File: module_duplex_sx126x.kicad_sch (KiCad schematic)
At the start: 34 parts, among them J1 USB_B_Mini, J2 Conn_01x08_Pin, J3 Conn_01x05, J4 Conn_01x04, J6 Conn_01x02, SW1 SW_Push, U1 STM32F103C8Tx, U2 AMS1117-3.3, U3 SN65HVD230, U4 Ai-Thinker-Ra-02, U5 Ai-Thinker-Ra-02, Y1 16M, Y2 32.768k

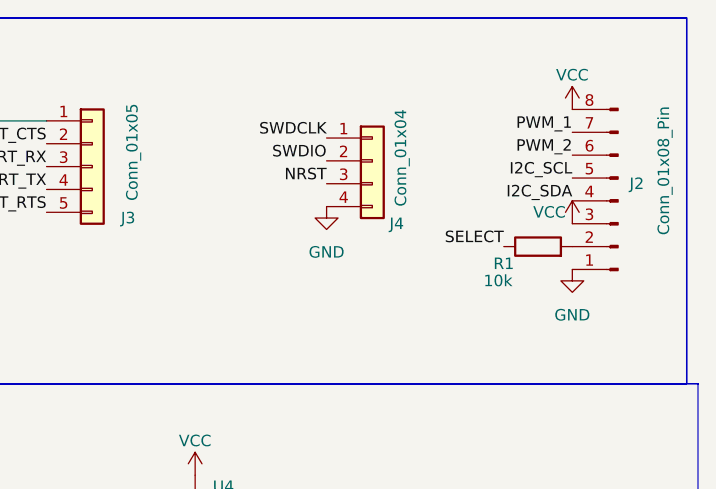
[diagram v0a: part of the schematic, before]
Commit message: Reduced expansion pins by simplifying select function with pull up/down
Signed-off-by: Leonardo Celente <leocelente@gmail.com>
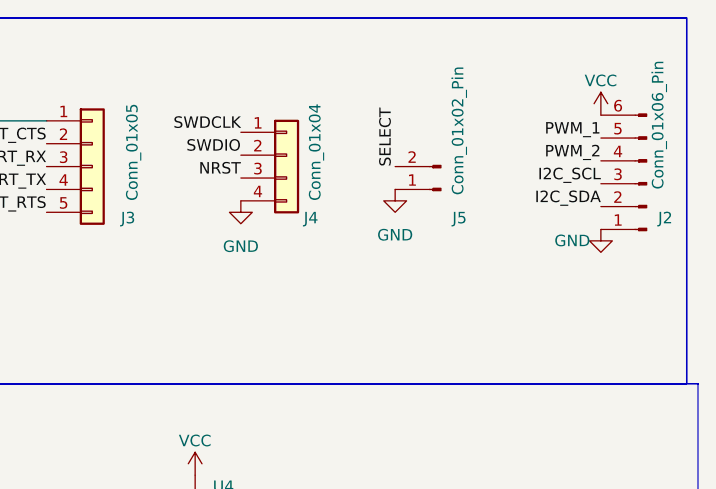
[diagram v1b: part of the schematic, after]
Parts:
- removed J2: Conn_01x08_Pin, Connector_PinHeader_2.54mm:PinHeader_1x08_P2.54mm_Vertical, symbol Connector:Conn_01x08_Pin
- removed R1: 10k, Resistor_SMD:R_0603_1608Metric, symbol Device:R
- added J2: Conn_01x06_Pin, Connector_PinHeader_2.54mm:PinHeader_1x06_P2.54mm_Vertical, symbol Connector:Conn_01x06_Pin
- added J5: Conn_01x02_Pin, Connector_PinHeader_2.54mm:PinHeader_1x02_P2.54mm_Vertical, symbol Connector:Conn_01x02_Pin
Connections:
- net GND: now also J2.1 (Pin_1), J5.1 (Pin_1)
- net I2C_SCL: now also J2.3 (Pin_3)
- net I2C_SDA: now also J2.2 (Pin_2)
- net PWM_1: now also J2.5 (Pin_5)
- net PWM_2: now also J2.4 (Pin_4)
- net SELECT: now also J5.2 (Pin_2)
- net VCC: now also J2.6 (Pin_6)
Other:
- moved on the sheet: J4

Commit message: Added USB resistors
Signed-off-by: Leonardo Celente <leocelente@gmail.com>
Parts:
- added R1, R4: 22, Resistor_SMD:R_0603_1608Metric, symbol Device:R
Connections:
- net USB_DM: now also R4.2; no longer J1.2 (D-)
- net USB_DP: now also R1.2; no longer J1.3 (D+)
- new net: J1.3 (D+), R1.1
- new net: J1.2 (D-), R4.1
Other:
- moved on the sheet: J1
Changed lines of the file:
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@@
   (no_connect (at 240.03 138.43))
   (no_connect (at 240.03 146.05))
-  (no_connect (at 119.38 43.18))
-  (no_connect (at 129.54 38.1))
+  (no_connect (at 111.125 43.18))
+  (no_connect (at 121.285 38.1))
   (no_connect (at 240.03 140.97))
   (no_connect (at 154.94 29.21))
@@
     (effects (font (size 1.27 1.27)) (justify right bottom))
   )
-  (label "USB_DM" (at 129.54 35.56 0) (fields_autoplaced)
+  (label "USB_DM" (at 128.905 35.56 0) (fields_autoplaced)
     (effects (font (size 1.27 1.27)) (justify left bottom))
   )
@@
     (effects (font (size 1.27 1.27)) (justify left bottom))
   )
-  (label "USB_DP" (at 129.54 33.02 0) (fields_autoplaced)
+  (label "USB_DP" (at 128.905 33.02 0) (fields_autoplaced)
     (effects (font (size 1.27 1.27)) (justify left bottom))
   )
@@
     )
   )
-  (symbol (lib_id "Connector:USB_B_Mini") (at 121.92 33.02 0) (unit 1)
+  (symbol (lib_id "Device:R") (at 125.095 33.02 90) (unit 1)
     (in_bom yes) (on_board yes) (dnp no) (fields_autoplaced)
-    (property "Reference" "J1" (at 121.92 21.59 0)
+    (property "Reference" "R1" (at 125.095 27.94 90)
       (effects (font (size 1.27 1.27)))
     )
-    (property "Value" "USB_B_Mini" (at 121.92 24.13 0)
+    (property "Value" "22" (at 125.095 30.48 90)
       (effects (font (size 1.27 1.27)))
     )
-    (property "Footprint" "Connector_USB:USB_Mini-B_Lumberg_2486_01_Horizontal" (at 125.73 34.29 0)
+    (property "Footprint" "Resistor_SMD:R_0603_1608Metric" (at 125.095 34.798 90)
       (effects (font (size 1.27 1.27)) hide)
     )
-    (property "Datasheet" "~" (at 125.73 34.29 0)
+    (property "Datasheet" "~" (at 125.095 33.02 0)
+      (effects (font (size 1.27 1.27)) hide)
+    )
+    (pin "1")
+    (pin "2")
+    (instances
+      (project "module_duplex_sx126x"
+        (path "/cad4c6e2-312a-4b4d-83a4-aea5cc498c0d"
+          (reference "R1") (unit 1)
+        )
+      )
+    )
+  )
+  (symbol (lib_id "Connector:USB_B_Mini") (at 113.665 33.02 0) (unit 1)
+    (in_bom yes) (on_board yes) (dnp no) (fields_autoplaced)
+    (property "Reference" "J1" (at 113.665 21.59 0)
+      (effects (font (size 1.27 1.27)))
+    )
+    (property "Value" "USB_B_Mini" (at 113.665 24.13 0)
+      (effects (font (size 1.27 1.27)))
+    )
+    (property "Footprint" "Connector_USB:USB_Mini-B_Lumberg_2486_01_Horizontal" (at 117.475 34.29 0)
+      (effects (font (size 1.27 1.27)) hide)
+    )
+    (property "Datasheet" "~" (at 117.475 34.29 0)
       (effects (font (size 1.27 1.27)) hide)
     )
@@
     )
   )
+  (symbol (lib_id "Device:R") (at 125.095 35.56 90) (unit 1)
+    (in_bom yes) (on_board yes) (dnp no)
+    (property "Reference" "R4" (at 124.46 38.1 90)
+      (effects (font (size 1.27 1.27)))
+    )
+    (property "Value" "22" (at 124.46 40.64 90)
+      (effects (font (size 1.27 1.27)))
+    )
+    (property "Footprint" "Resistor_SMD:R_0603_1608Metric" (at 125.095 37.338 90)
+      (effects (font (size 1.27 1.27)) hide)
+    )
+    (property "Datasheet" "~" (at 125.095 35.56 0)
+      (effects (font (size 1.27 1.27)) hide)
+    )
+    (pin "1")
+    (pin "2")
+    (instances
+      (project "module_duplex_sx126x"
+        (path "/cad4c6e2-312a-4b4d-83a4-aea5cc498c0d"
+          (reference "R4") (unit 1)
+        )
+      )
+    )
+  )
   (symbol (lib_id "Device:C") (at 33.02 149.86 90) (unit 1)
     (in_bom yes) (on_board yes) (dnp no)
@@
     )
   )
-  (symbol (lib_id "power:VBUS") (at 129.54 27.94 0) (unit 1)
+  (symbol (lib_id "power:VBUS") (at 121.285 27.94 0) (unit 1)
     (in_bom yes) (on_board yes) (dnp no)
-    (property "Reference" "#PWR011" (at 129.54 31.75 0)
+    (property "Reference" "#PWR011" (at 121.285 31.75 0)
       (effects (font (size 1.27 1.27)) hide)
     )
-    (property "Value" "VBUS" (at 132.08 24.13 0)
+    (property "Value" "VBUS" (at 123.825 24.13 0)
       (effects (font (size 1.27 1.27)))
     )
-    (property "Footprint" "" (at 129.54 27.94 0)
+    (property "Footprint" "" (at 121.285 27.94 0)
       (effects (font (size 1.27 1.27)) hide)
     )
-    (property "Datasheet" "" (at 129.54 27.94 0)
+    (property "Datasheet" "" (at 121.285 27.94 0)
       (effects (font (size 1.27 1.27)) hide)
     )
@@
     )
   )
-  (symbol (lib_id "power:GND") (at 121.92 43.18 0) (unit 1)
+  (symbol (lib_id "power:GND") (at 113.665 43.18 0) (unit 1)
     (in_bom yes) (on_board yes) (dnp no)
-    (property "Reference" "#PWR012" (at 121.92 49.53 0)
+    (property "Reference" "#PWR012" (at 113.665 49.53 0)
       (effects (font (size 1.27 1.27)) hide)
     )
-    (property "Value" "GND" (at 121.92 48.26 0)
+    (property "Value" "GND" (at 113.665 48.26 0)
       (effects (font (size 1.27 1.27)))
     )
-    (property "Footprint" "" (at 121.92 43.18 0)
+    (property "Footprint" "" (at 113.665 43.18 0)
       (effects (font (size 1.27 1.27)) hide)
     )
-    (property "Datasheet" "" (at 121.92 43.18 0)
+    (property "Datasheet" "" (at 113.665 43.18 0)
       (effects (font (size 1.27 1.27)) hide)
     )

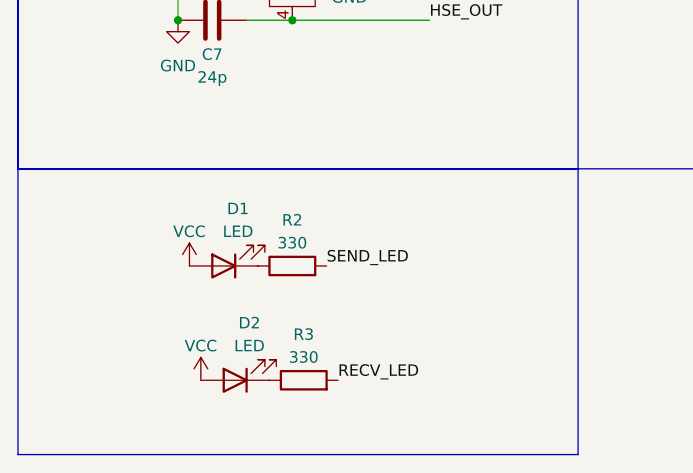
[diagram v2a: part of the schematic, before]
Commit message: Added power indicator LED
Signed-off-by: Leonardo Celente <leocelente@gmail.com>
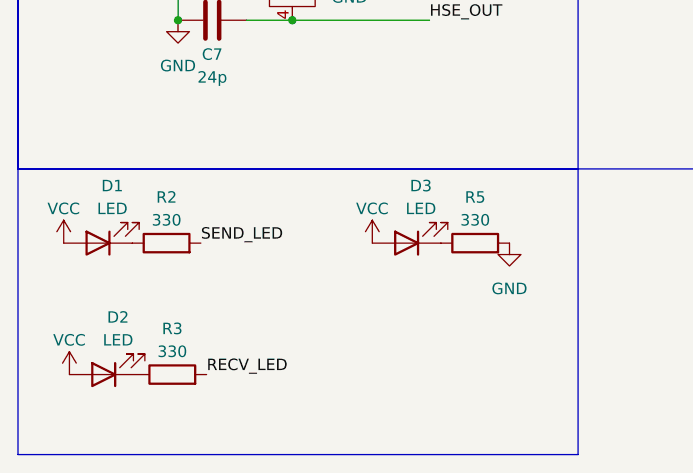
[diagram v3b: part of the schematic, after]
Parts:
- added D3: LED, LED_SMD:LED_0603_1608Metric, symbol Device:LED
- added R5: 330, Resistor_SMD:R_0603_1608Metric, symbol Device:R
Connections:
- net GND: now also R5.2
- net VCC: now also D3.2 (A)
- new net: D3.1 (K), R5.1
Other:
- moved on the sheet: D1, D2, R2, R3

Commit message: First Pass routing top copper layer
Signed-off-by: Leonardo Celente <leocelente@gmail.com>
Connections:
- net UART_RTS: now also J3.3 (Pin_3); no longer J3.5 (Pin_5)
- net UART_RX: now also J3.5 (Pin_5); no longer J3.3 (Pin_3)
- net CONN_DP: now reaches J1.3 (D+), R1.1
- net CONN_DN: now reaches J1.2 (D-), R4.1
- net USB_DM renamed USB_DN
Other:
- moved on the sheet: R1, R4
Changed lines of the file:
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@@
+    (stroke (width 0) (type default))
+  )
+  (wire (pts (xy 121.285 33.02) (xy 123.825 33.02))
     (stroke (width 0) (type default))
   )
@@
   )
   (wire (pts (xy 41.91 38.1) (xy 53.34 38.1))
+    (stroke (width 0) (type default))
+  )
+  (wire (pts (xy 121.285 35.56) (xy 123.825 35.56))
     (stroke (width 0) (type default))
   )
@@
     (effects (font (size 1.27 1.27)) (justify right bottom))
   )
-  (label "USB_DM" (at 128.905 35.56 0) (fields_autoplaced)
+  (label "USB_DN" (at 131.445 35.56 0) (fields_autoplaced)
     (effects (font (size 1.27 1.27)) (justify left bottom))
   )
@@
     (effects (font (size 1.27 1.27)) (justify right bottom))
   )
+  (label "CONN_DN" (at 123.825 35.56 270) (fields_autoplaced)
+    (effects (font (size 1.27 1.27)) (justify right bottom))
+  )
   (label "RADIO_RECV_SCK" (at 219.71 81.28 180) (fields_autoplaced)
     (effects (font (size 1.27 1.27)) (justify right bottom))
@@
     (effects (font (size 1.27 1.27)) (justify left bottom))
   )
-  (label "UART_RX" (at 213.36 29.21 180) (fields_autoplaced)
+  (label "UART_RX" (at 213.36 34.29 180) (fields_autoplaced)
     (effects (font (size 1.27 1.27)) (justify right bottom))
   )
@@
     (effects (font (size 1.27 1.27)) (justify right bottom))
   )
-  (label "USB_DM" (at 139.7 100.33 0) (fields_autoplaced)
+  (label "USB_DN" (at 139.7 100.33 0) (fields_autoplaced)
     (effects (font (size 1.27 1.27)) (justify left bottom))
   )
@@
     (effects (font (size 1.27 1.27)) (justify left bottom))
   )
+  (label "CONN_DP" (at 123.825 33.02 90) (fields_autoplaced)
+    (effects (font (size 1.27 1.27)) (justify left bottom))
+  )
   (label "UART_RX" (at 139.7 80.01 0) (fields_autoplaced)
     (effects (font (size 1.27 1.27)) (justify left bottom))
@@
     (effects (font (size 1.27 1.27)) (justify left bottom))
   )
-  (label "UART_RTS" (at 213.36 34.29 180) (fields_autoplaced)
+  (label "UART_RTS" (at 213.36 29.21 180) (fields_autoplaced)
     (effects (font (size 1.27 1.27)) (justify right bottom))
   )
@@
     (effects (font (size 1.27 1.27)) (justify left bottom))
   )
-  (label "USB_DP" (at 128.905 33.02 0) (fields_autoplaced)
+  (label "USB_DP" (at 131.445 33.02 0) (fields_autoplaced)
     (effects (font (size 1.27 1.27)) (justify left bottom))
   )
@@
     )
   )
-  (symbol (lib_id "Device:R") (at 125.095 33.02 90) (unit 1)
+  (symbol (lib_id "Device:R") (at 127.635 33.02 90) (unit 1)
     (in_bom yes) (on_board yes) (dnp no) (fields_autoplaced)
-    (property "Reference" "R1" (at 125.095 27.94 90)
-      (effects (font (size 1.27 1.27)))
-    )
-    (property "Value" "22" (at 125.095 30.48 90)
-      (effects (font (size 1.27 1.27)))
-    )
-    (property "Footprint" "Resistor_SMD:R_0603_1608Metric" (at 125.095 34.798 90)
-      (effects (font (size 1.27 1.27)) hide)
-    )
-    (property "Datasheet" "~" (at 125.095 33.02 0)
+    (property "Reference" "R1" (at 127.635 27.94 90)
+      (effects (font (size 1.27 1.27)))
+    )
+    (property "Value" "22" (at 127.635 30.48 90)
+      (effects (font (size 1.27 1.27)))
+    )
+    (property "Footprint" "Resistor_SMD:R_0603_1608Metric" (at 127.635 34.798 90)
+      (effects (font (size 1.27 1.27)) hide)
+    )
+    (property "Datasheet" "~" (at 127.635 33.02 0)
       (effects (font (size 1.27 1.27)) hide)
     )
@@
     )
   )
-  (symbol (lib_id "Device:R") (at 125.095 35.56 90) (unit 1)
+  (symbol (lib_id "Device:R") (at 127.635 35.56 90) (unit 1)
     (in_bom yes) (on_board yes) (dnp no)
-    (property "Reference" "R4" (at 124.46 38.1 90)
-      (effects (font (size 1.27 1.27)))
-    )
-    (property "Value" "22" (at 124.46 40.64 90)
-      (effects (font (size 1.27 1.27)))
-    )
-    (property "Footprint" "Resistor_SMD:R_0603_1608Metric" (at 125.095 37.338 90)
-      (effects (font (size 1.27 1.27)) hide)
-    )
-    (property "Datasheet" "~" (at 125.095 35.56 0)
-      (effects (font (size 1.27 1.27)) hide)
-    )
+    (property "Reference" "R4" (at 127 38.1 90)
+      (effects (font (size 1.27 1.27)))
+    )
+    (property "Value" "22" (at 127 40.64 90)
+      (effects (font (size 1.27 1.27)))
+    )
+    (property "Footprint" "Resistor_SMD:R_0603_1608Metric" (at 127.635 37.338 90)
+      (effects (font (size 1.27 1.27)) hide)
+    )
+    (property "Datasheet" "~" (at 127.635 35.56 0)
+      (effects (font (size 1.27 1.27)) hide)
+    )

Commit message: First Pass of full layout
Signed-off-by: Leonardo Celente <leocelente@gmail.com>
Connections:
- net GND: now also J1.6 (Shield)
- no-connect marks 13 -> 12
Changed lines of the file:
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@@
   (junction (at 21.59 38.1) (diameter 0) (color 0 0 0 0)
+  )
+  (junction (at 113.665 43.18) (diameter 0) (color 0 0 0 0)
   )
   (junction (at 121.92 67.31) (diameter 0) (color 0 0 0 0)
@@
   (no_connect (at 240.03 138.43))
   (no_connect (at 240.03 146.05))
-  (no_connect (at 111.125 43.18))
   (no_connect (at 121.285 38.1))
   (no_connect (at 240.03 140.97))
@@
   )
   (wire (pts (xy 29.21 144.78) (xy 29.21 149.86))
+    (stroke (width 0) (type default))
+  )
+  (wire (pts (xy 111.125 43.18) (xy 113.665 43.18))
     (stroke (width 0) (type default))
   )
@@
       (effects (font (size 1.27 1.27)) hide)
     )
-    (property "Value" "VBUS" (at 123.825 24.13 0)
-      (effects (font (size 1.27 1.27)))
-    )
+    (property "Value" "VBUS" (at 121.158 22.606 90)
+      (effects (font (size 1.27 1.27)))
+    )
